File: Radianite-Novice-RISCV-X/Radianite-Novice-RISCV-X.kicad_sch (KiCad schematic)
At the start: 131 parts, among them J1 USB_C_Receptacle_USB2.0_16P, J2 Conn_01x10_Pin, J3 Conn_01x08_Pin, J4 Conn_01x08, J5 Conn_01x06, J6 Barrel_Jack_Switch, J7 Radianite-Link, SW1 SW_Push, U1 CH32V305RBT6, U2 ESP32-C3-WROOM-02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

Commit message: a lot of commit shit lol (PROJECT LEMON IRVINE FUCKED UP)
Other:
- moved on the sheet: C7, C8, R1, Y1
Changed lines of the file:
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@@
 	)
 	(junction
-		(at 344.17 158.75)
+		(at 288.29 110.49)
 		(diameter 0)
 		(color 0 0 0 0)
@@
 	)
 	(junction
-		(at 339.09 162.56)
+		(at 292.1 115.57)
 		(diameter 0)
 		(color 0 0 0 0)
@@
 	)
 	(junction
-		(at 344.17 166.37)
+		(at 295.91 110.49)
 		(diameter 0)
 		(color 0 0 0 0)
@@
 	)
 	(junction
-		(at 320.04 162.56)
+		(at 292.1 134.62)
 		(diameter 0)
 		(color 0 0 0 0)
@@
 	(wire
 		(pts
-			(xy 332.74 166.37) (xy 344.17 166.37)
+			(xy 295.91 121.92) (xy 295.91 110.49)
 		)
 		(stroke
@@
 	(wire
 		(pts
-			(xy 325.12 166.37) (xy 320.04 166.37)
+			(xy 295.91 129.54) (xy 295.91 134.62)
 		)
 		(stroke
@@
 	(wire
 		(pts
-			(xy 339.09 162.56) (xy 349.25 162.56)
+			(xy 292.1 115.57) (xy 292.1 105.41)
 		)
 		(stroke
@@
 	(wire
 		(pts
-			(xy 320.04 166.37) (xy 320.04 162.56)
+			(xy 295.91 134.62) (xy 292.1 134.62)
 		)
 		(stroke
@@
 	(wire
 		(pts
-			(xy 320.04 162.56) (xy 339.09 162.56)
+			(xy 292.1 134.62) (xy 292.1 115.57)
 		)
 		(stroke
@@
 	(wire
 		(pts
-			(xy 356.87 158.75) (xy 359.41 158.75)
+			(xy 288.29 97.79) (xy 288.29 95.25)
 		)
 		(stroke
@@
 	(wire
 		(pts
-			(xy 344.17 166.37) (xy 359.41 166.37)
+			(xy 295.91 110.49) (xy 295.91 95.25)
 		)
 		(stroke
@@
 	(wire
 		(pts
-			(xy 332.74 158.75) (xy 344.17 158.75)
+			(xy 288.29 121.92) (xy 288.29 110.49)
 		)
 		(stroke
@@
 	(wire
 		(pts
-			(xy 325.12 158.75) (xy 320.04 158.75)
+			(xy 288.29 129.54) (xy 288.29 134.62)
 		)
 		(stroke
@@
 	(wire
 		(pts
-			(xy 344.17 158.75) (xy 349.25 158.75)
+			(xy 288.29 110.49) (xy 288.29 105.41)
 		)
 		(stroke
@@
 	(wire
 		(pts
-			(xy 320.04 158.75) (xy 320.04 162.56)
+			(xy 288.29 134.62) (xy 292.1 134.62)
 		)
 		(stroke
@@
 	)
 	(label "XIN"
-		(at 359.41 158.75 0)
+		(at 288.29 95.25 90)
 		(fields_autoplaced yes)
 		(effects
@@
 	)
 	(label "XOUT"
-		(at 359.41 166.37 0)
+		(at 295.91 95.25 90)
 		(fields_autoplaced yes)
 		(effects
@@
 	(symbol
 		(lib_id "Device:C")
-		(at 328.93 166.37 270)
+		(at 295.91 125.73 0)
 		(unit 1)
 		(exclude_from_sim no)
@@
 		(dnp no)
 		(property "Reference" "C8"
-			(at 328.93 170.434 90)
+			(at 299.974 125.73 90)
 			(effects
 				(font
@@
 		)
 		(property "Value" "20pF"
-			(at 328.93 172.974 90)
+			(at 302.514 125.73 90)
 			(effects
 				(font
@@
 		)
 		(property "Footprint" "Capacitor_SMD:C_0402_1005Metric"
-			(at 325.12 167.3352 0)
+			(at 296.8752 129.54 0)
 			(effects
 				(font
@@
 		)
 		(property "Datasheet" "~"
-			(at 328.93 166.37 0)
+			(at 295.91 125.73 0)
 			(effects
 				(font
@@
 		)
 		(property "Description" "Unpolarized capacitor"
-			(at 328.93 166.37 0)
+			(at 295.91 125.73 0)
 			(effects
 				(font
@@
 	(symbol
 		(lib_id "power:GND")
-		(at 320.04 162.56 270)
+		(at 292.1 134.62 0)
 		(unit 1)
 		(exclude_from_sim no)
@@
 		(fields_autoplaced yes)
 		(property "Reference" "#PWR04"
-			(at 313.69 162.56 0)
+			(at 292.1 140.97 0)
 			(effects
 				(font
@@
 		)
 		(property "Value" "GND"
-			(at 316.23 162.5599 90)
+			(at 292.0999 138.43 90)
 			(effects
 				(font
@@
 		)
 		(property "Footprint" ""
-			(at 320.04 162.56 0)
+			(at 292.1 134.62 0)
 			(effects
 				(font
@@
 		)
 		(property "Datasheet" ""
-			(at 320.04 162.56 0)
+			(at 292.1 134.62 0)
 			(effects
 				(font
@@
 		)
 		(property "Description" "Power symbol creates a global label with name \"GND\" , ground"
-			(at 320.04 162.56 0)
+			(at 292.1 134.62 0)
 			(effects
 				(font
@@
 	(symbol
 		(lib_id "Device:Crystal_GND24")
-		(at 344.17 162.56 270)
+		(at 292.1 110.49 0)
 		(unit 1)
 		(exclude_from_sim no)
@@
 		(dnp no)
 		(property "Reference" "Y1"
-			(at 335.28 150.114 90)
+			(at 279.654 119.38 90)
 			(effects
 				(font
@@
 		)
 		(property "Value" "8MHz"
-			(at 336.296 152.654 90)
+			(at 282.194 118.364 90)
 			(effects
 				(font
@@
 		)
 		(property "Footprint" "Crystal:Crystal_SMD_3225-4Pin_3.2x2.5mm"
-			(at 344.17 162.56 0)
+			(at 292.1 110.49 0)
 			(effects
 				(font
@@
 		)
 		(property "Datasheet" "~"
-			(at 344.17 162.56 0)
+			(at 292.1 110.49 0)
 			(effects
 				(font
@@
 		)
 		(property "Description" "Four pin crystal, GND on pins 2 and 4"
-			(at 344.17 162.56 0)
+			(at 292.1 110.49 0)
 			(effects
 				(font
@@
 		)
 		(property "a" "CF4008M00012001"
-			(at 342.9 155.1626 90)
+			(at 284.7026 111.76 90)
 			(effects
 				(font
@@
 	(symbol
 		(lib_id "Device:R")
-		(at 353.06 158.75 90)
+		(at 288.29 101.6 180)
 		(unit 1)
 		(exclude_from_sim no)
@@
 		(dnp no)
 		(property "Reference" "R1"
-			(at 353.06 156.718 90)
+			(at 286.258 101.6 90)
 			(effects
 				(font
@@
 		)
 		(property "Value" "40"
-			(at 353.06 158.75 90)
+			(at 288.29 101.6 90)
 			(effects
 				(font
@@
 		)
 		(property "Footprint" "Resistor_SMD:R_0402_1005Metric"
-			(at 353.06 160.528 90)
+			(at 290.068 101.6 90)
 			(effects
 				(font
@@
 		)
 		(property "Datasheet" "~"
-			(at 353.06 158.75 0)
+			(at 288.29 101.6 0)
 			(effects
 				(font
@@
 		)
 		(property "Description" "Resistor"
-			(at 353.06 158.75 0)
+			(at 288.29 101.6 0)
 			(effects
 				(font
@@
 	(symbol
 		(lib_id "Device:C")
-		(at 328.93 158.75 90)
+		(at 288.29 125.73 180)
 		(unit 1)
 		(exclude_from_sim no)
@@
 		(fields_autoplaced yes)
 		(property "Reference" "C7"
-			(at 328.93 151.13 90)
+			(at 280.67 125.73 90)
 			(effects
 				(font
@@
 		)
 		(property "Value" "20pF"
-			(at 328.93 153.67 90)
+			(at 283.21 125.73 90)
 			(effects
 				(font
@@
 		)
 		(property "Footprint" "Capacitor_SMD:C_0402_1005Metric"
-			(at 332.74 157.7848 0)
+			(at 287.3248 121.92 0)
 			(effects
 				(font
@@
 		)
 		(property "Datasheet" "~"
-			(at 328.93 158.75 0)
+			(at 288.29 125.73 0)
 			(effects
 				(font
@@
 		)
 		(property "Description" "Unpolarized capacitor"
-			(at 328.93 158.75 0)
+			(at 288.29 125.73 0)
 			(effects
 				(font

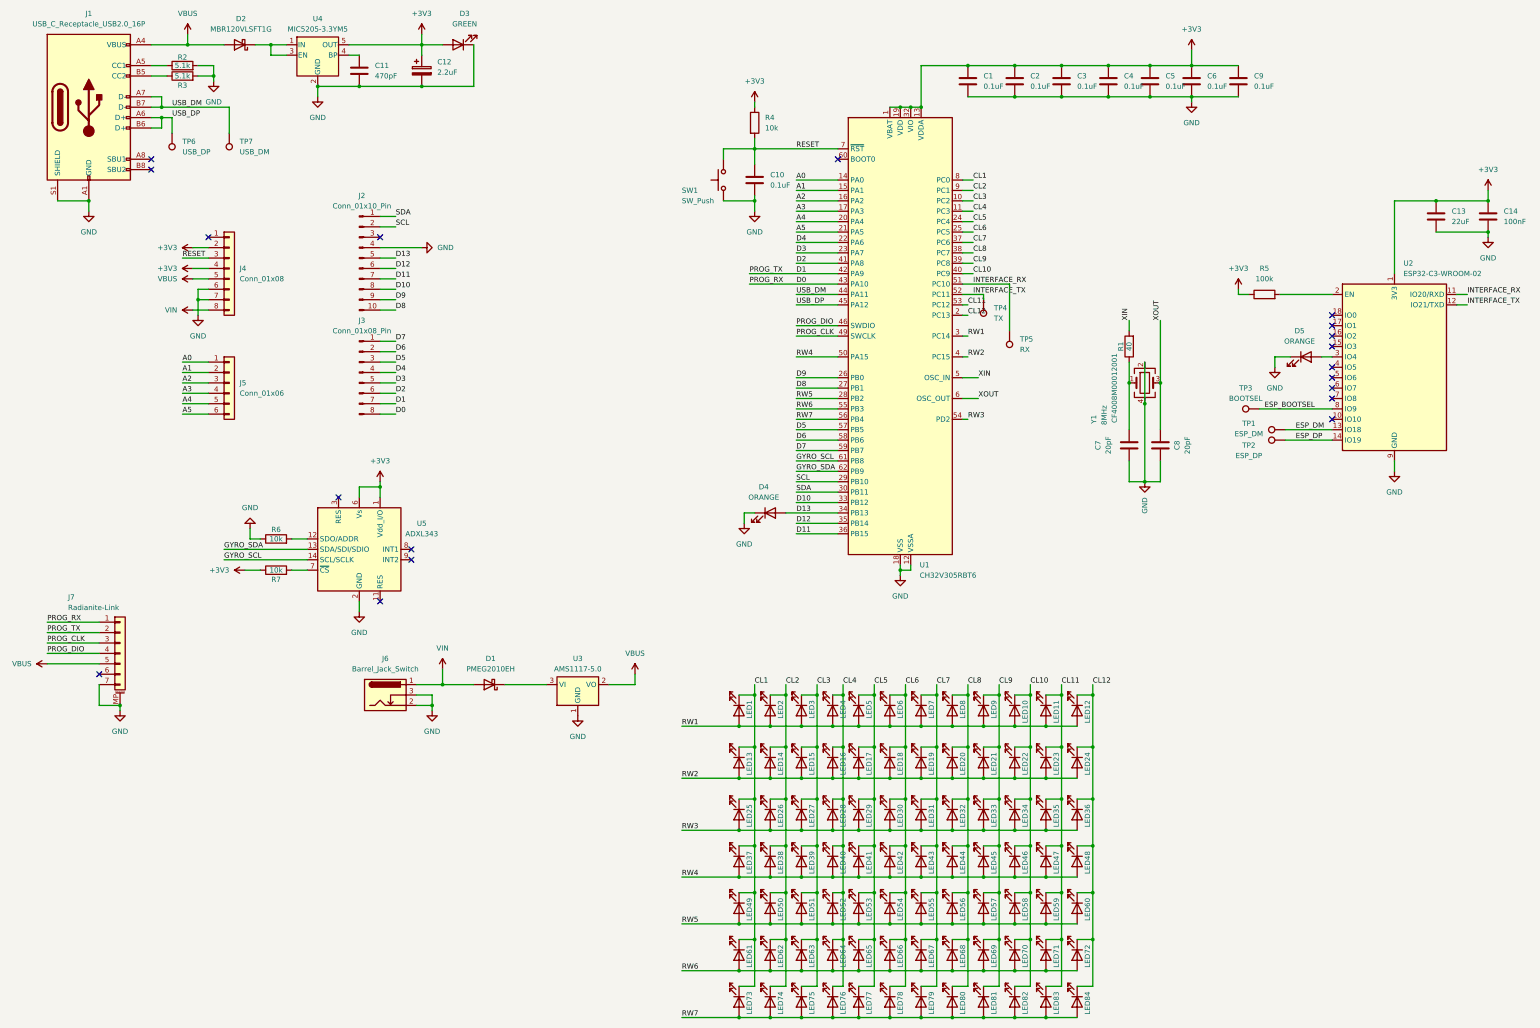
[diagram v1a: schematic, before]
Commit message: fix some pcb (major rev, see on https://www.reddit.com/r/PrintedCircuitBoard/comments/1fpfia7/review_request_arduino_uno_r4_wifi_clone_using/)
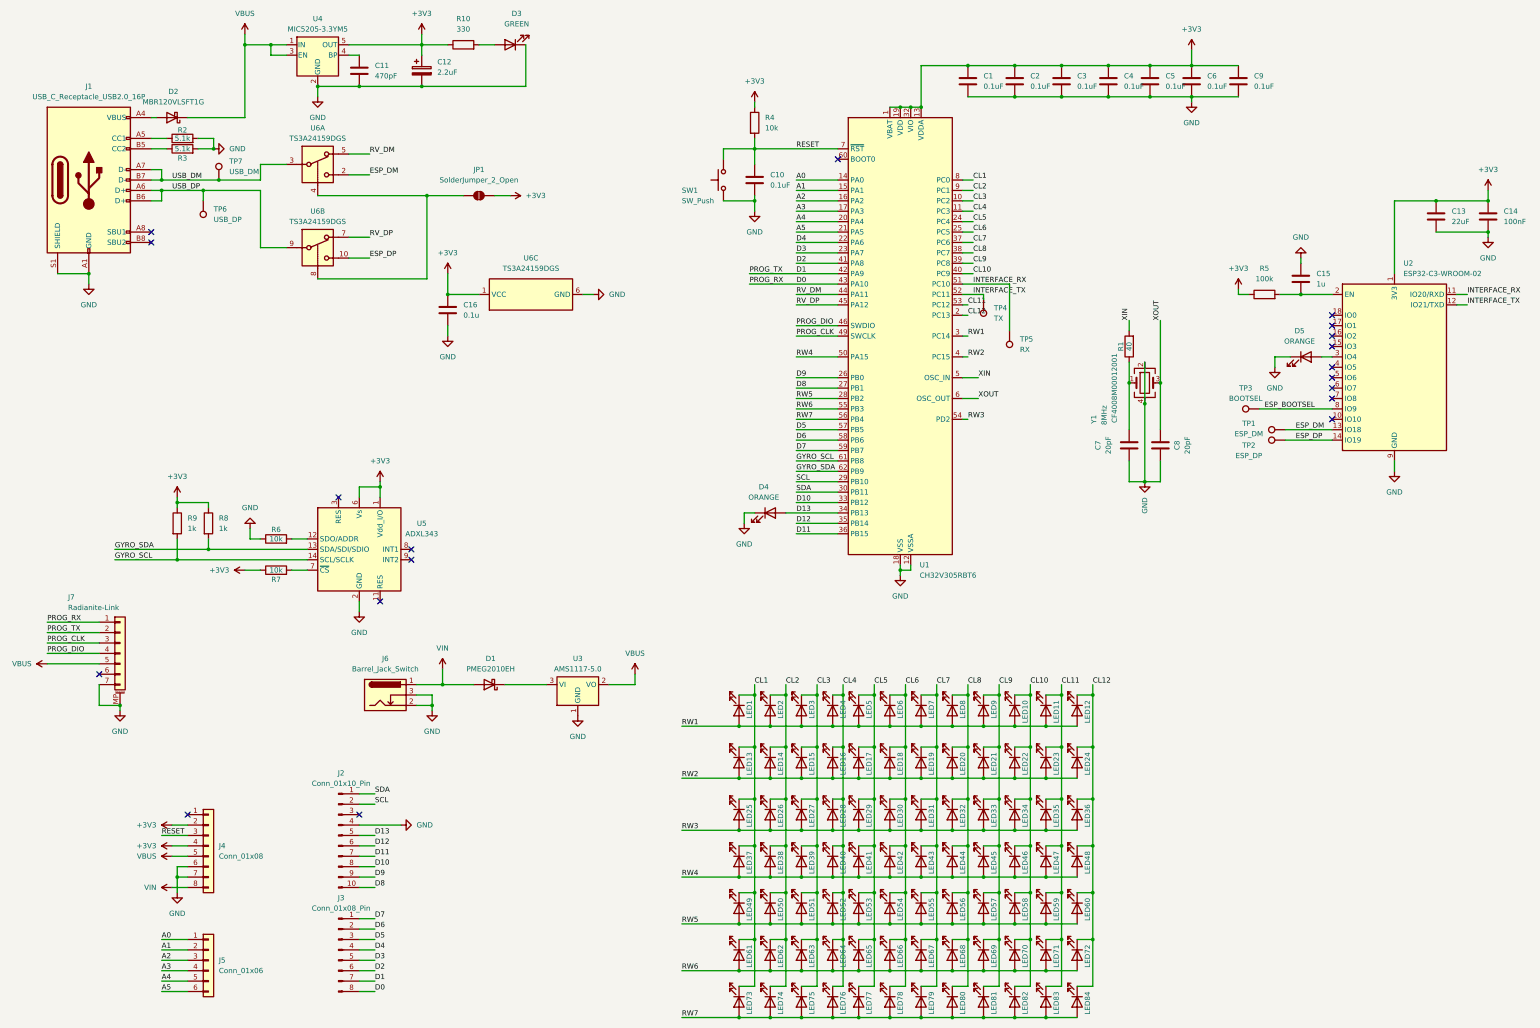
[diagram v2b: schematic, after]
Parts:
- added C15: 1u, Capacitor_SMD:C_0402_1005Metric, symbol Device:C
- added C16: 0.1u, Capacitor_SMD:C_0603_1608Metric, symbol Device:C
- added JP1: SolderJumper_2_Open, Jumper:SolderJumper-2_P1.3mm_Open_RoundedPad1.0x1.5mm, symbol Jumper:SolderJumper_2_Open
- added R10: 330, Resistor_SMD:R_0402_1005Metric, symbol Device:R
- added R8, R9: 1k, Resistor_SMD:R_0402_1005Metric, symbol Device:R
- added U6: TS3A24159DGS, Package_SO:TSSOP-10_3x3mm_P0.5mm, symbol Analog_Switch:TS3A24159DGS
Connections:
- net +3V3: now also C16.1, JP1.2 (B), R10.1, R8.1, R9.1, U6.1 (VCC); no longer D3.2 (A)
- net ESP_DM: now also U6.2
- net ESP_DP: now also U6.10
- net GND: now also C15.1, C16.2, U6.6 (GND)
- net GYRO_SCL: now also R9.2
- net GYRO_SDA: now also R8.2
- net USB_DM: now also U6.3; no longer U1.44 (PA11)
- net USB_DP: now also U6.9; no longer U1.45 (PA12)
- net VBUS: now also D2.1 (K), U4.1 (IN), U4.3 (EN); no longer D2.2 (A), J1.A4 (VBUS), J1.A9 (VBUS), J1.B4 (VBUS), J1.B9 (VBUS)
- net at R5.2, U2.2 (EN): now also C15.2
- new net: JP1.1 (A), U6.4, U6.8
- new net: D3.2 (A), R10.2
- new net: D2.2 (A), J1.A4 (VBUS), J1.A9 (VBUS), J1.B4 (VBUS), J1.B9 (VBUS)
- new net RV_DM: U1.44 (PA11), U6.5
- new net RV_DP: U1.45 (PA12), U6.7
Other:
- moved on the sheet: D2, D3, J1, J2, J3, J4, J5, R2, R3, TP6, TP7

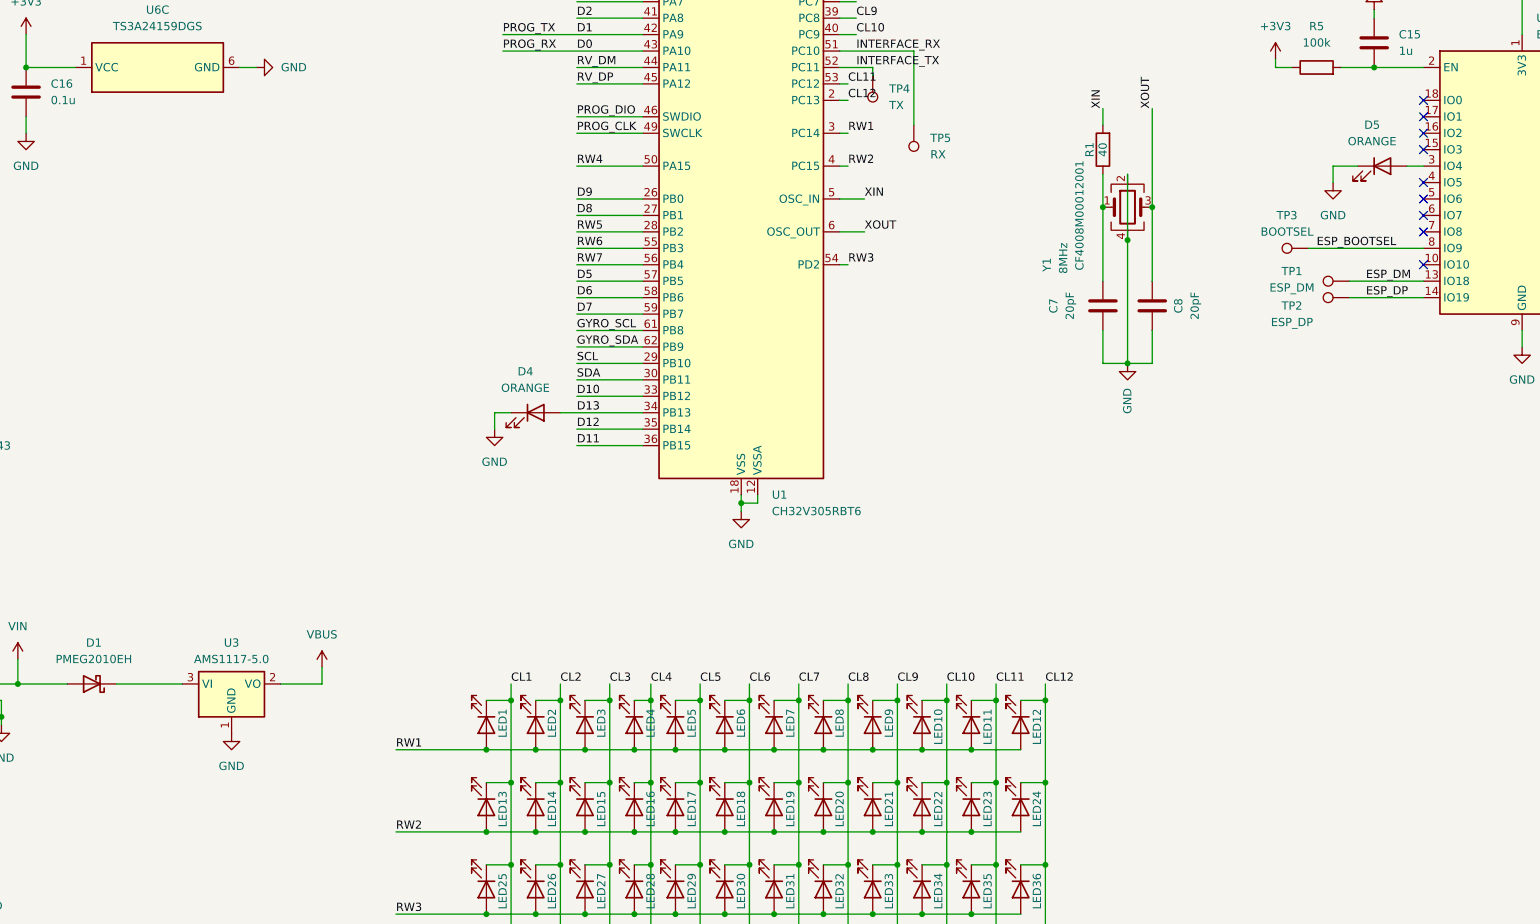
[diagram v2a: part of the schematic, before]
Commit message: fix some stuff violating clearances and adding current limiting resistor
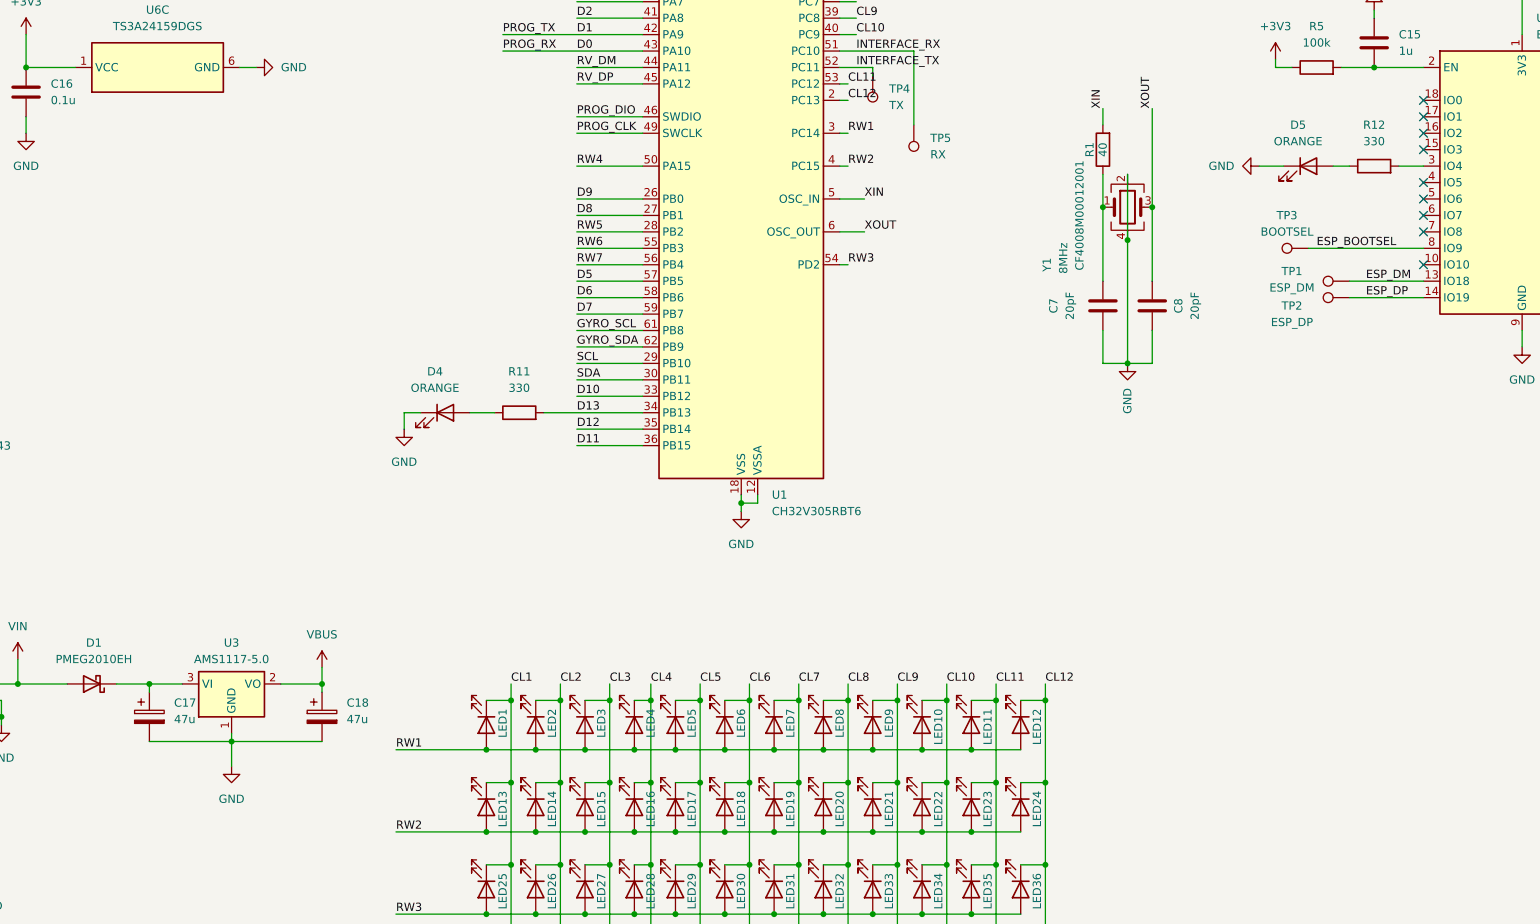
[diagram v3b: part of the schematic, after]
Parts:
- added C17, C18: 47u, Capacitor_SMD:CP_Elec_3x5.3, symbol Device:C_Polarized
- added R11, R12: 330, Resistor_SMD:R_0402_1005Metric, symbol Device:R
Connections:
- net D13: now also R11.2; no longer D4.2 (A)
- net GND: now also C17.2, C18.2
- net VBUS: now also C18.1
- net at D1.1 (K), U3.3 (VI): now also C17.1
- net at U2.3 (IO4): now also R12.2; no longer D5.2 (A)
- new net: D4.2 (A), R11.1
- new net: D5.2 (A), R12.1
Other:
- moved on the sheet: D4, D5
